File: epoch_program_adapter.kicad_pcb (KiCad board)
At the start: 4 copper layers, 28 x 8.2 mm, 8 parts, among them J1 CONN_02X05, J2 CONN_01X05, Q1 DMP1045U, U1 LTC4412

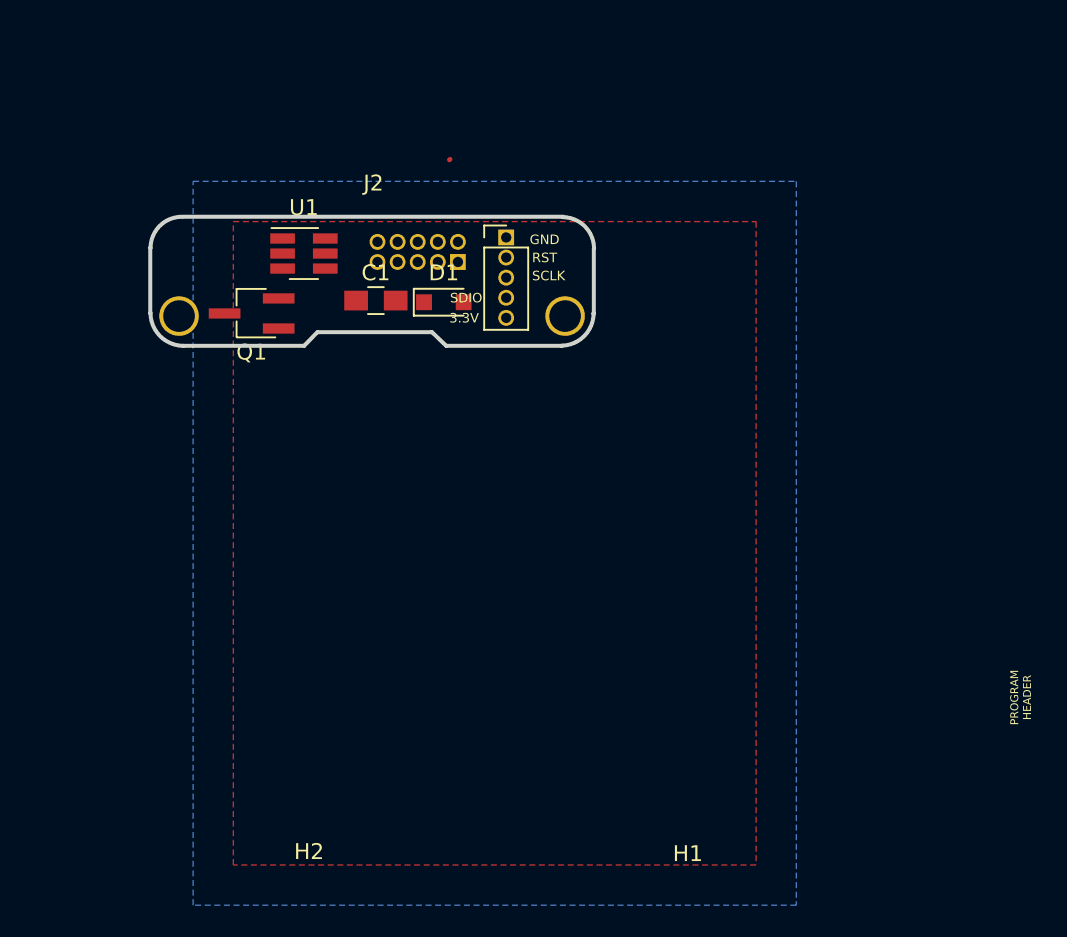
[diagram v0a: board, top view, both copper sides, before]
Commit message: Increase drill size to 2.1.  Rework daughter board
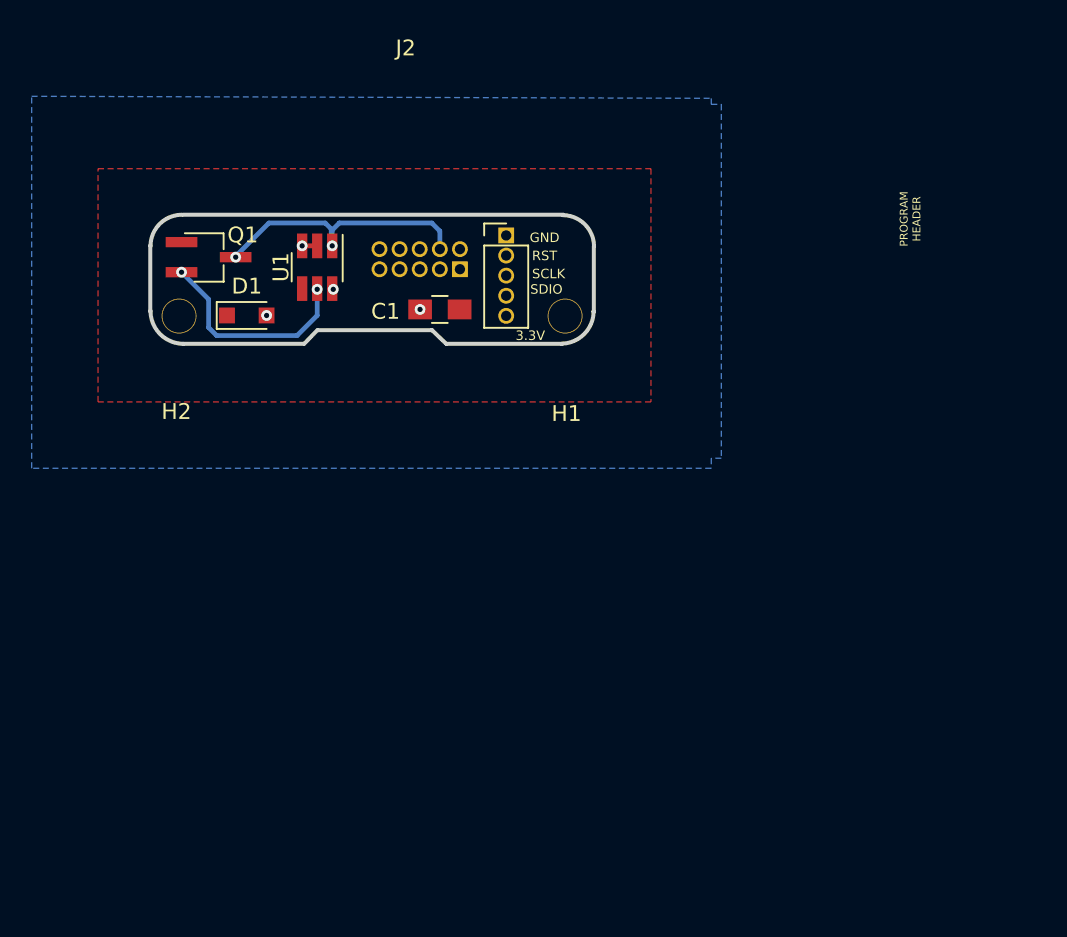
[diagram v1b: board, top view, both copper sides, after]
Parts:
- H1, H2: footprint my-fp-library:MH2mm -> my-fp-library:MH2.1mm
- moved H2 30.9 mm to (103.0, 86.4)
- moved H1 30.8 mm to (127.6, 86.6)
- moved D1 12.5 mm to (107.4, 86.6)
- moved Q1 4.48 mm to (105.0, 82.9), turned to 0 degrees
- moved C1 4.08 mm to (119.6, 86.2)
- moved U1 1.20 mm to (111.8, 83.5), turned to 270 degrees
- moved J1 0.47 mm to (120.9, 83.7)
- moved J2 0.13 mm to (123.8, 81.5)
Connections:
- C1 pad 2: (+3.3V) -> +3V3
- D1 pad 1: (+3.3V) -> +3V3
- J1 pad 1: VCC -> +3V3
- J1 pad 3: GND -> (GND)
- J1 pad 5: GND -> (GND)
- J2 pad 1: GND -> (GND)
- J2 pad 5: VCC -> +3V3
- Q1 pad 1: (+3.3V) -> +3V3
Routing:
- net SWDIO/+3.3V(REGUL): track 0.00 -> 28.8 mm, vias 0 -> 2
- net SWDCLK/+3.3V(BATT): track 0.00 -> 24.3 mm, vias 0 -> 2
- net Net-(Q1-Pad2): track 0.00 -> 13.5 mm, vias 0 -> 2
- net RESET: track 0.00 -> 10.0 mm
- net (GND): track 0.00 -> 1.05 mm, vias 0 -> 2
- added copper zone on F.Cu, net +3V3
- removed copper zone on F.Cu, net (+3.3)

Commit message: V2.0 - Manufactured Board and Adapter
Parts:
- moved H1 0.13 mm to (127.6, 86.4)
- moved H2 0.13 mm to (103.0, 86.3)
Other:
- outline, holes or cut-outs redrawn
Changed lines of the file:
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@@
     (links 17)
     (no_connects 0)
-    (area 101.180999 80.086199 129.463801 88.493601)
+    (area 89.583124 67.485123 150.214 99.8716)
     (thickness 1.6002)
-    (drawings 19)
+    (drawings 20)
     (tracks 60)
     (zones 0)
@@
   )
   (setup
-    (last_trace_width 0.1524)
+    (last_trace_width 0.254)
     (user_trace_width 0.15)
     (user_trace_width 0.2)
@@
   )
   (module my-fp-library:MH2.1mm (layer F.Cu)
-    (at 127.597 86.576)
-    (fp_text reference H1 (at 0 6.2) (layer F.SilkS)
+    (at 127.597 86.449)
+    (fp_text reference H1 (at -0.05588 0.06604) (layer F.SilkS)
       (effects (font (size 1 1) (thickness 0.15)))
     )
@@
   )
   (module my-fp-library:MH2.1mm (layer F.Cu)
-    (at 102.959 86.449)
-    (fp_text reference H2 (at 0 6.2) (layer F.SilkS)
+    (at 102.959 86.322)
+    (fp_text reference H2 (at 0.1016 0.19304) (layer F.SilkS)
       (effects (font (size 1 1) (thickness 0.15)))
     )
@@
     (pad 1 thru_hole circle (at 0.165 0.165) (size 2.2 2.2) (drill 2.1) (layers *.Cu *.Mask))
   )
+  (gr_line (start 126.835 82.385) (end 126.835 80.226) (angle 90) (layer Edge.Cuts) (width 0.254))
+  (gr_line (start 129.33436 82.385) (end 126.835 82.385) (angle 90) (layer Edge.Cuts) (width 0.254))
   (gr_line (start 129.3242 86.322) (end 129.2988 86.322) (angle 90) (layer Edge.Cuts) (width 0.254))
-  (gr_line (start 129.3242 82.2072) (end 129.3242 86.322) (angle 90) (layer Edge.Cuts) (width 0.254))
-  (gr_line (start 101.308 82.1564) (end 101.308 86.322) (angle 90) (layer Edge.Cuts) (width 0.254))
+  (gr_line (start 129.32928 82.37992) (end 129.3242 86.322) (angle 90) (layer Edge.Cuts) (width 0.254))
+  (gr_line (start 101.3206 82.1564) (end 101.3206 86.322) (angle 90) (layer Edge.Cuts) (width 0.254))
   (gr_text "PROGRAM\nHEADER" (at 149.314 80.48 90) (layer F.SilkS)
     (effects (font (size 0.5 0.5) (thickness 0.125)))
@@
   (gr_arc (start 103.4034 86.2838) (end 103.378 88.3666) (angle 89.30130562) (layer Edge.Cuts) (width 0.254))
   (gr_arc (start 127.25654 86.30158) (end 129.3114 86.31936) (angle 88.09506312) (layer Edge.Cuts) (width 0.254))
-  (gr_arc (start 127.3556 82.2198) (end 127.3556 80.2386) (angle 90) (layer Edge.Cuts) (width 0.254))
   (gr_arc (start 103.3018 82.1944) (end 101.3206 82.1944) (angle 90) (layer Edge.Cuts) (width 0.254))
   (gr_line (start 120.015 88.3666) (end 127.30734 88.3666) (angle 90) (layer Edge.Cuts) (width 0.254))
@@
     (effects (font (size 0.6 0.6) (thickness 0.125)))
   )
-  (gr_text GND (at 126.2126 81.661) (layer F.SilkS)
+  (gr_text GND (at 126.00188 81.27756 90) (layer F.SilkS)
     (effects (font (size 0.6 0.6) (thickness 0.125)))
   )
-  (gr_line (start 103.378 80.2132) (end 127.4064 80.2132) (angle 90) (layer Edge.Cuts) (width 0.254))
+  (gr_line (start 103.2892 80.21584) (end 126.835 80.2132) (angle 90) (layer Edge.Cuts) (width 0.254))
   (segment (start 123.787 82.7914) (end 123.5584 82.7914) (width 0.3) (layer In2.Cu) (net 1))
   (segment (start 123.5584 82.7914) (end 121.628 80.861) (width 0.3) (layer In2.Cu) (net 1))

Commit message: V3
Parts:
- added J3: CONN_01X02, Pin_Headers:Pin_Header_Straight_1x02_Pitch1.27mm, F.Cu at (108.0, 86.9)
- moved D1 1.85 mm to (105.6, 86.1), turned to 90 degrees
- moved Q1 0.81 mm to (105.5, 82.3)
- moved J1 0.38 mm to (120.5, 83.7)
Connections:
- D1 pad 2: SWDIO/+3.3V(REGUL) -> +3.3V(REGUL)
- J1 pad 2: SWDIO/+3.3V(REGUL) -> SWDIO
- J1 pad 4: SWDCLK/+3.3V(BATT) -> SWDCLK
- J2 pad 3: SWDCLK/+3.3V(BATT) -> SWDCLK
- J2 pad 4: SWDIO/+3.3V(REGUL) -> SWDIO
- Q1 pad 3: SWDCLK/+3.3V(BATT) -> +3.3V(BATT)
- U1 pad 1: SWDCLK/+3.3V(BATT) -> +3.3V(BATT)
- U1 pad 6: SWDIO/+3.3V(REGUL) -> +3.3V(REGUL)
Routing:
- net SWDIO/+3.3V(REGUL): track 28.8 -> 0.00 mm, vias 2 -> 0
- net SWDCLK/+3.3V(BATT): track 24.3 -> 0.00 mm, vias 2 -> 0
- net +3.3V(BATT): track 0.00 -> 17.9 mm, vias 0 -> 2
- net +3.3V(REGUL): track 0.00 -> 9.67 mm, vias 0 -> 2
- net SWDCLK: track 0.00 -> 6.93 mm
- net SWDIO: track 0.00 -> 5.56 mm
- net Net-(Q1-Pad2): track 13.5 -> 9.05 mm
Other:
- board text added: "BATT"
- board text added: "REG"
